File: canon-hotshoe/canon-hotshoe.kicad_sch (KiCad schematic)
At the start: 11 parts, among them J1 PogoPin, J10 PogoPin, J11 PogoPin, J2 PogoPin, J3 PogoPin, J4 PogoPin, J5 PogoPin, J6 PogoPin, J7 PogoPin, J8 PogoPin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

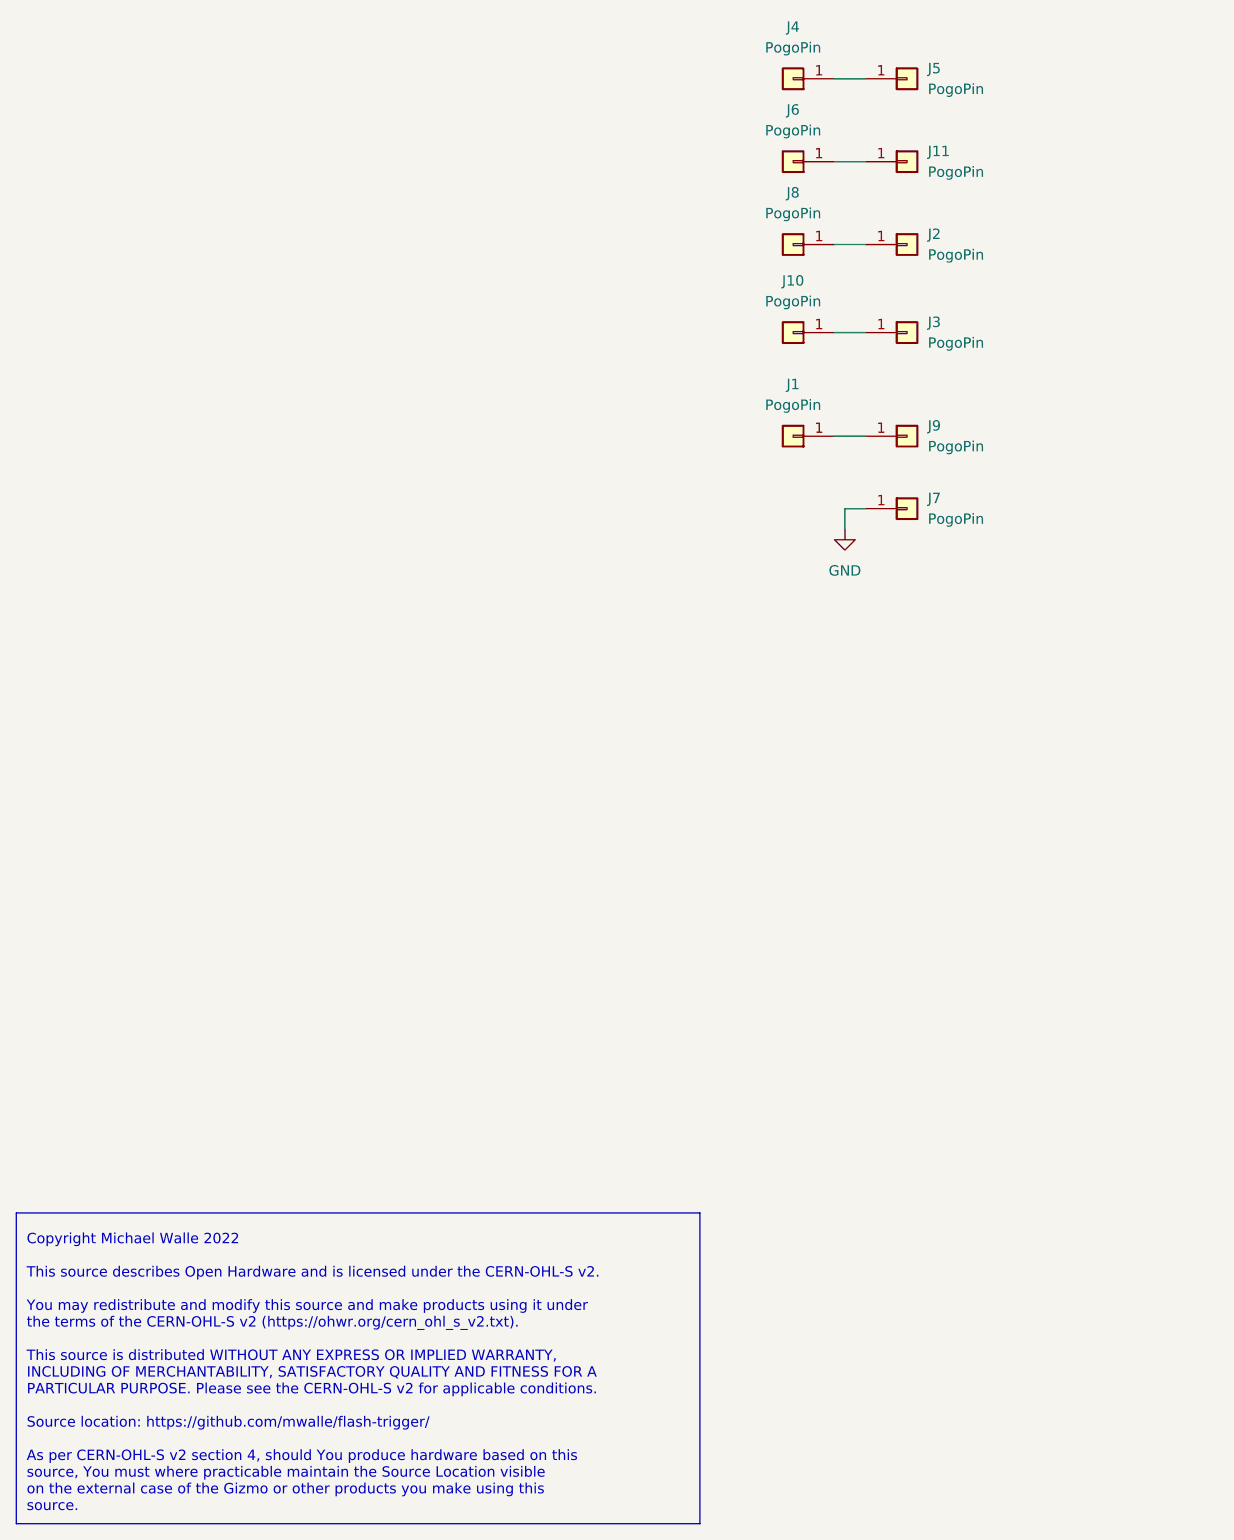
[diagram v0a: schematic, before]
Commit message: Fixes and improvements
 * fix the preflash detection
 * clean the canon hot shoe schematics up
 * enlarge the hotshoe pcb and place two new mounting pins
 * change the battery low to a battery good detection
 * move the supervisor ic away from the hot shoe rail
 * use a longer pogo pin
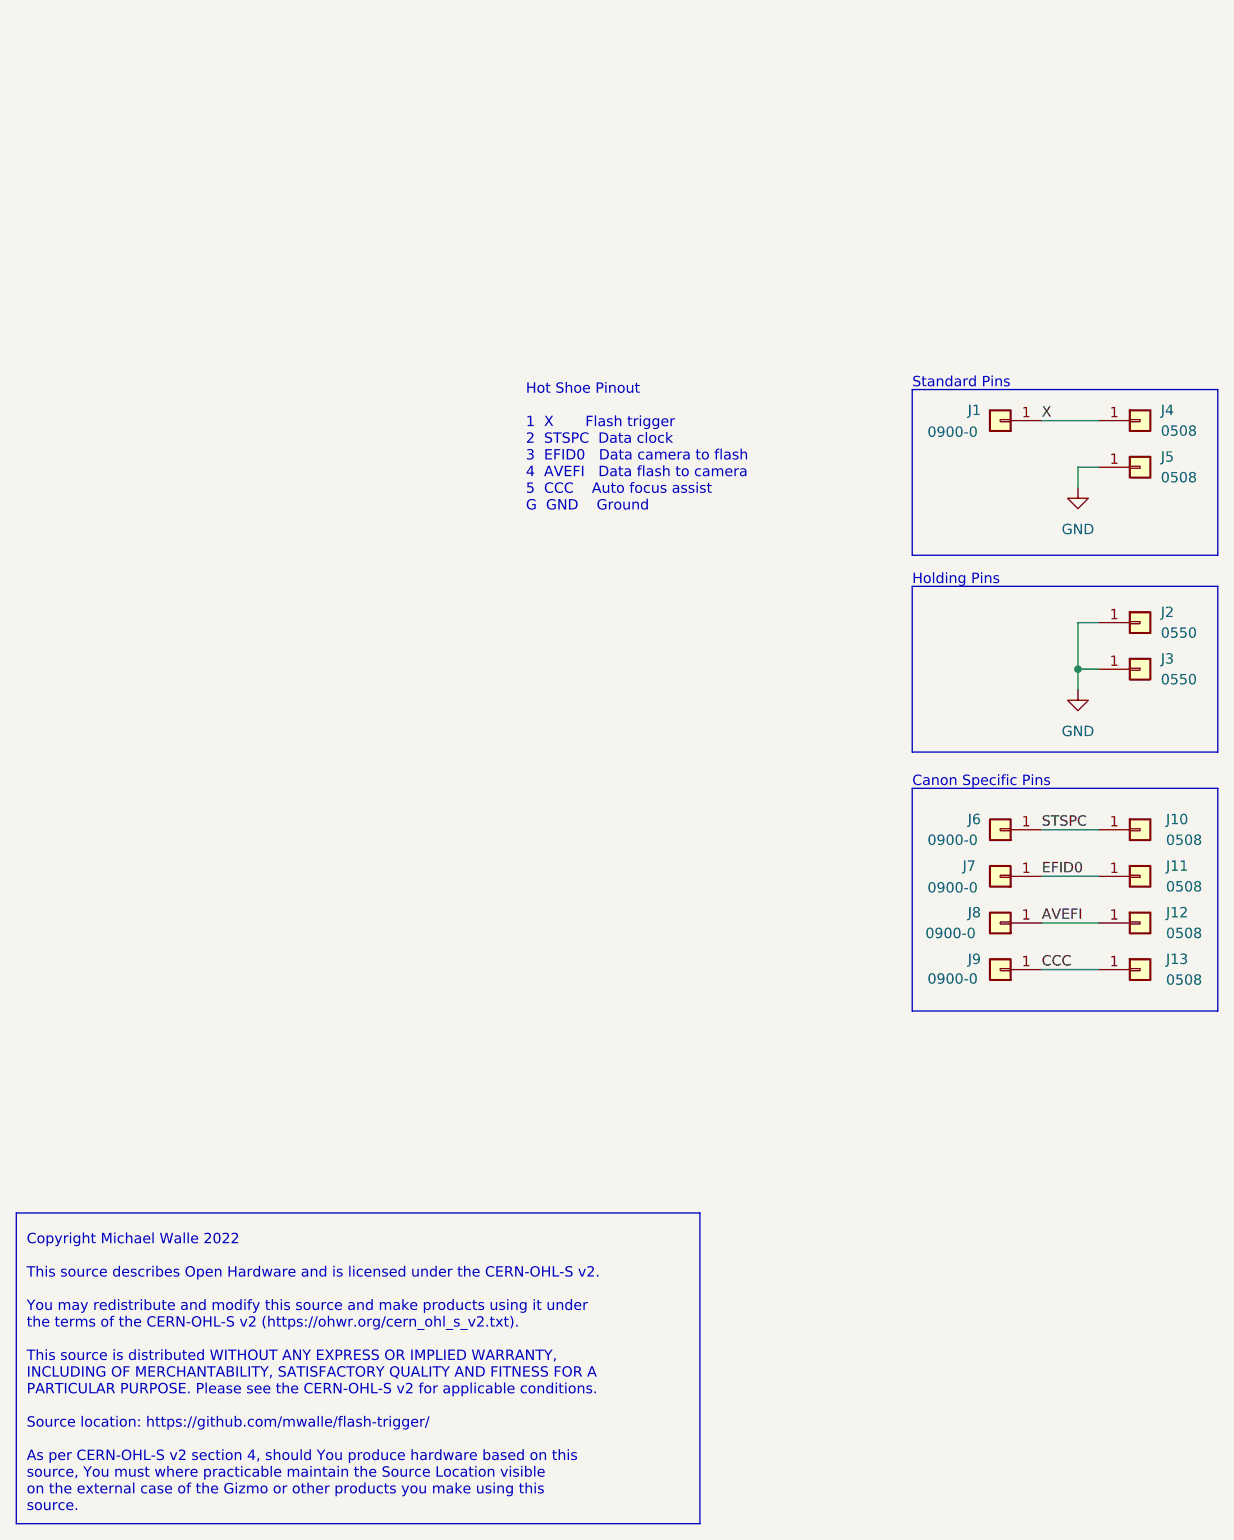
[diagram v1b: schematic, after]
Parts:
- added J2, J3: 0550, Connector_MillMax:0550_52mil, symbol Connector_Pin:Pin
- J1: value PogoPin -> 0900-0; footprint Connector_MillMax:0965_1.65mm_Reverse -> Connector_MillMax:0900-0_137mil_Reverse
- J10: renamed from J5; value PogoPin -> 0508
- J11: renamed from J3; value PogoPin -> 0508
- J12: renamed from J11; value PogoPin -> 0508
- J13: renamed from J2; value PogoPin -> 0508
- J4: renamed from J9; value PogoPin -> 0508
- J5: renamed from J7; value PogoPin -> 0508
- J6: renamed from J4; value PogoPin -> 0900-0; footprint Connector_MillMax:0965_1.65mm_Reverse -> Connector_MillMax:0900-0_137mil_Reverse
- J7: renamed from J10; value PogoPin -> 0900-0; footprint Connector_MillMax:0965_1.65mm_Reverse -> Connector_MillMax:0900-0_137mil_Reverse
- J8: renamed from J6; value PogoPin -> 0900-0; footprint Connector_MillMax:0965_1.65mm_Reverse -> Connector_MillMax:0900-0_137mil_Reverse
- J9: renamed from J8; value PogoPin -> 0900-0; footprint Connector_MillMax:0965_1.65mm_Reverse -> Connector_MillMax:0900-0_137mil_Reverse
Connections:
- net GND: now also J2.1 (Pin_1), J3.1 (Pin_1)
- net X: now reaches J1.1 (Pin_1), J4.1 (Pin_1)
- net AVEFI: now reaches J12.1 (Pin_1), J8.1 (Pin_1)
- net STSPC: now reaches J10.1 (Pin_1), J6.1 (Pin_1)
- net CCC: now reaches J13.1 (Pin_1), J9.1 (Pin_1)
- net EFID0: now reaches J11.1 (Pin_1), J7.1 (Pin_1)
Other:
- note added: "Canon Specific Pins"
- note added: "Holding Pins"
- note added: "Hot Shoe Pinout 1 X Flash trigger 2 STSPC Data clock 3 EFID0 Data camera to flash 4 AVEFI Data flash to camera 5 CCC Auto focus assist G GND Ground"
- note added: "Standard Pins"
- moved on the sheet: J1, J10, J11, J12, J13, J4, J5, J6, J7, J8, J9
